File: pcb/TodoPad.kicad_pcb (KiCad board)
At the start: 2 copper layers, 30 parts, among them SW1 SW_Push, SW10 SW_Push, SW11 SW_Push, SW12 SW_Push, SW13 SW_Push, SW14 SW_Push, SW2 SW_Push, SW3 SW_Push, SW4 SW_Push, SW5 SW_Push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

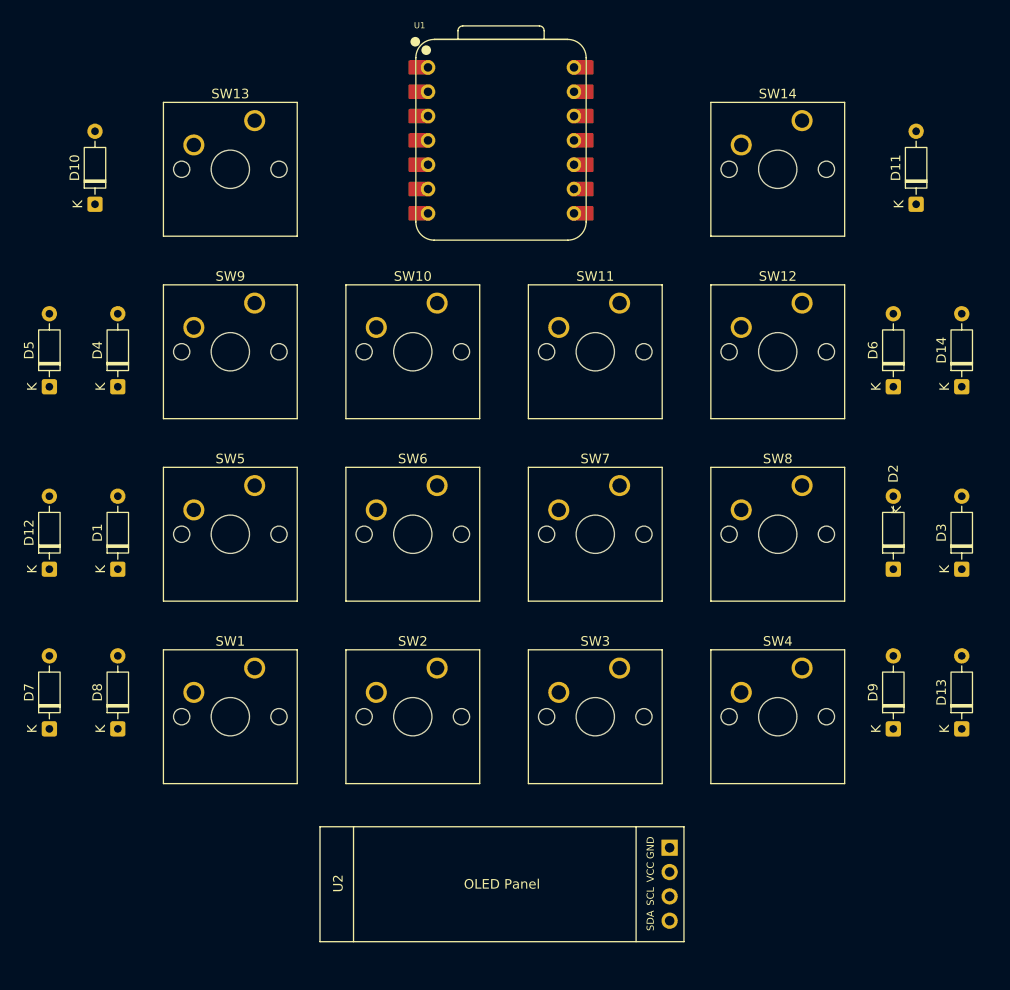
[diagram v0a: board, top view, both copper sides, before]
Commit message: Started routing PCB
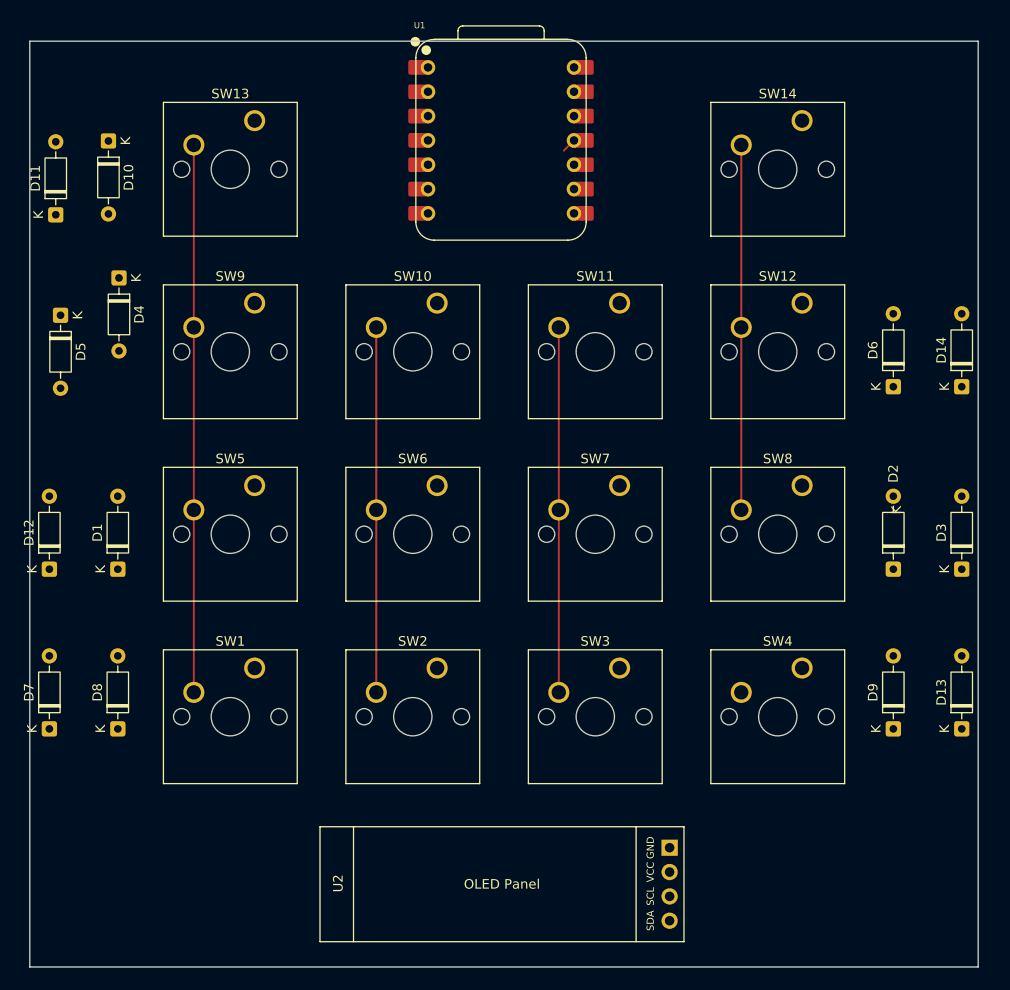
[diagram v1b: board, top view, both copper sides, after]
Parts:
- moved D11 89.8 mm to (92.7, 64.6)
- moved D4 11.4 mm to (99.3, 71.2), turned to -90 degrees
- moved D5 7.55 mm to (93.2, 75.1), turned to -90 degrees
- moved D10 6.76 mm to (98.2, 56.9), turned to -90 degrees
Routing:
- net Col 0: track 0.00 -> 58.7 mm
- net Col 3: track 0.00 -> 38.5 mm
- net Col 2: track 0.00 -> 38.1 mm
- net Col 1: track 0.00 -> 38.1 mm
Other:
- board outline added: 99 x 96.7 mm
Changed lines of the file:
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@@
 	(footprint "Diode_THT:D_DO-35_SOD27_P7.62mm_Horizontal"
 		(layer "F.Cu")
-		(at 99.1775 82.55 90)
+		(at 99.3 71.19 -90)
 		(descr "Diode, DO-35_SOD27 series, Axial, Horizontal, pin pitch=7.62mm, length*diameter=4*2mm^2, http://www.diodes.com/_files/packages/DO-35.pdf")
 		(tags "Diode DO-35_SOD27 series Axial Horizontal pin pitch 7.62mm  length 4mm diameter 2mm")
@@
 		)
 		(property "Sim.Device" "D"
-			(at 0 0 90)
+			(at 0 0 270)
 			(unlocked yes)
 			(layer "F.Fab")
@@
 		)
 		(property "Sim.Pins" "1=K 2=A"
-			(at 0 0 90)
+			(at 0 0 270)
 			(unlocked yes)
 			(layer "F.Fab")
@@
 		(attr through_hole)
 		(fp_line
-			(start 2.53 -1.12)
-			(end 2.53 1.12)
+			(start 1.04 0)
+			(end 1.69 0)
 			(stroke
 				(width 0.12)
@@
 		)
 		(fp_line
-			(start 2.41 -1.12)
-			(end 2.41 1.12)
+			(start 6.58 0)
+			(end 5.93 0)
 			(stroke
 				(width 0.12)
@@
 		)
 		(fp_line
-			(start 6.58 0)
-			(end 5.93 0)
+			(start 2.41 -1.12)
+			(end 2.41 1.12)
 			(stroke
 				(width 0.12)
@@
 		)
 		(fp_line
-			(start 1.04 0)
-			(end 1.69 0)
+			(start 2.53 -1.12)
+			(end 2.53 1.12)
 			(stroke
 				(width 0.12)
@@
 		)
 		(fp_line
-			(start 2.51 -1)
-			(end 2.51 1)
+			(start 0 0)
+			(end 1.81 0)
 			(stroke
 				(width 0.1)
@@
 		)
 		(fp_line
-			(start 2.41 -1)
-			(end 2.41 1)
+			(start 7.62 0)
+			(end 5.81 0)
 			(stroke
 				(width 0.1)
@@
 		)
 		(fp_line
-			(start 7.62 0)
-			(end 5.81 0)
+			(start 2.41 -1)
+			(end 2.41 1)
 			(stroke
 				(width 0.1)
@@
 		)
 		(fp_line
-			(start 0 0)
-			(end 1.81 0)
+			(start 2.51 -1)
+			(end 2.51 1)
 			(stroke
 				(width 0.1)
@@
 		)
 		(pad "1" thru_hole roundrect
-			(at 0 0 90)
+			(at 0 0 270)
 			(size 1.6 1.6)
 			(drill 0.8)
@@
 		)
 		(pad "2" thru_hole circle
-			(at 7.62 0 90)
+			(at 7.62 0 270)
 			(size 1.6 1.6)
 			(drill 0.8)
@@
 	(footprint "Diode_THT:D_DO-35_SOD27_P7.62mm_Horizontal"
 		(layer "F.Cu")
-		(at 96.79625 63.5 90)
+		(at 98.2 56.89 -90)
 		(descr "Diode, DO-35_SOD27 series, Axial, Horizontal, pin pitch=7.62mm, length*diameter=4*2mm^2, http://www.diodes.com/_files/packages/DO-35.pdf")
 		(tags "Diode DO-35_SOD27 series Axial Horizontal pin pitch 7.62mm  length 4mm diameter 2mm")
@@
 		)
 		(property "Sim.Device" "D"
-			(at 0 0 90)
+			(at 0 0 270)
 			(unlocked yes)
 			(layer "F.Fab")
@@
 		)
 		(property "Sim.Pins" "1=K 2=A"
-			(at 0 0 90)
+			(at 0 0 270)
 			(unlocked yes)
 			(layer "F.Fab")
@@
 		(attr through_hole)
 		(fp_line
-			(start 2.53 -1.12)
-			(end 2.53 1.12)
+			(start 1.04 0)
+			(end 1.69 0)
 			(stroke
 				(width 0.12)
@@
 		)
 		(fp_line
-			(start 2.41 -1.12)
-			(end 2.41 1.12)
+			(start 6.58 0)
+			(end 5.93 0)
 			(stroke
 				(width 0.12)
@@
 		)
 		(fp_line
-			(start 6.58 0)
-			(end 5.93 0)
+			(start 2.41 -1.12)
+			(end 2.41 1.12)
 			(stroke
 				(width 0.12)
@@
 		)
 		(fp_line
-			(start 1.04 0)
-			(end 1.69 0)
+			(start 2.53 -1.12)
+			(end 2.53 1.12)
 			(stroke
 				(width 0.12)
@@
 		)
 		(fp_line
-			(start 2.51 -1)
-			(end 2.51 1)
+			(start 0 0)
+			(end 1.81 0)
 			(stroke
 				(width 0.1)
@@
 		)
 		(fp_line
-			(start 2.41 -1)
-			(end 2.41 1)
+			(start 7.62 0)
+			(end 5.81 0)
 			(stroke
 				(width 0.1)
@@
 		)
 		(fp_line
-			(start 7.62 0)
-			(end 5.81 0)
+			(start 2.41 -1)
+			(end 2.41 1)
 			(stroke
 				(width 0.1)
@@
 		)
 		(fp_line
-			(start 0 0)
-			(end 1.81 0)
+			(start 2.51 -1)
+			(end 2.51 1)
 			(stroke
 				(width 0.1)
@@
 		)
 		(pad "1" thru_hole roundrect
-			(at 0 0 90)
+			(at 0 0 270)
 			(size 1.6 1.6)
 			(drill 0.8)
@@
 		)
 		(pad "2" thru_hole circle
-			(at 7.62 0 90)
+			(at 7.62 0 270)
 			(size 1.6 1.6)
 			(drill 0.8)
@@
 	(footprint "Diode_THT:D_DO-35_SOD27_P7.62mm_Horizontal"
 		(layer "F.Cu")
-		(at 182.52125 63.5 90)
+		(at 92.7 64.6 90)
 		(descr "Diode, DO-35_SOD27 series, Axial, Horizontal, pin pitch=7.62mm, length*diameter=4*2mm^2, http://www.diodes.com/_files/packages/DO-35.pdf")
 		(tags "Diode DO-35_SOD27 series Axial Horizontal pin pitch 7.62mm  length 4mm diameter 2mm")
@@
 	(footprint "Diode_THT:D_DO-35_SOD27_P7.62mm_Horizontal"
 		(layer "F.Cu")
-		(at 92.03375 82.55 90)
+		(at 93.2 75.09 -90)
 		(descr "Diode, DO-35_SOD27 series, Axial, Horizontal, pin pitch=7.62mm, length*diameter=4*2mm^2, http://www.diodes.com/_files/packages/DO-35.pdf")
 		(tags "Diode DO-35_SOD27 series Axial Horizontal pin pitch 7.62mm  length 4mm diameter 2mm")
@@
 		)
 		(property "Sim.Device" "D"
-			(at 0 0 90)
+			(at 0 0 270)
 			(unlocked yes)
 			(layer "F.Fab")
@@
 		)
 		(property "Sim.Pins" "1=K 2=A"
-			(at 0 0 90)
+			(at 0 0 270)
 			(unlocked yes)
 			(layer "F.Fab")
@@
 		(attr through_hole)
 		(fp_line
-			(start 2.53 -1.12)
-			(end 2.53 1.12)
+			(start 1.04 0)
+			(end 1.69 0)
 			(stroke
 				(width 0.12)
@@
 		)
 		(fp_line
-			(start 2.41 -1.12)
-			(end 2.41 1.12)
+			(start 6.58 0)
+			(end 5.93 0)
 			(stroke
 				(width 0.12)
@@
 		)
 		(fp_line
-			(start 6.58 0)
-			(end 5.93 0)
+			(start 2.41 -1.12)
+			(end 2.41 1.12)
 			(stroke
 				(width 0.12)
@@
 		)
 		(fp_line
-			(start 1.04 0)
-			(end 1.69 0)
+			(start 2.53 -1.12)
+			(end 2.53 1.12)
 			(stroke
 				(width 0.12)
@@
 		)
 		(fp_line
-			(start 2.51 -1)
-			(end 2.51 1)
+			(start 0 0)
+			(end 1.81 0)
 			(stroke
 				(width 0.1)
@@
 		)
 		(fp_line
-			(start 2.41 -1)
-			(end 2.41 1)
+			(start 7.62 0)
+			(end 5.81 0)
 			(stroke
 				(width 0.1)
@@
 		)
 		(fp_line
-			(start 7.62 0)
-			(end 5.81 0)
+			(start 2.41 -1)
+			(end 2.41 1)
 			(stroke
 				(width 0.1)
@@
 		)
 		(fp_line
-			(start 0 0)
-			(end 1.81 0)
+			(start 2.51 -1)
+			(end 2.51 1)
 			(stroke
 				(width 0.1)
@@
 		)
 		(pad "1" thru_hole roundrect
-			(at 0 0 90)
+			(at 0 0 270)
 			(size 1.6 1.6)
 			(drill 0.8)
@@
 		)
 		(pad "2" thru_hole circle
-			(at 7.62 0 90)
+			(at 7.62 0 270)
 			(size 1.6 1.6)
 			(drill 0.8)
@@
 		)
 	)
+	(gr_rect
+		(start 89.9875 46.475)
+		(end 189 143.125)
+		(stroke
+			(width 0.05)
+			(type default)
+		)
+		(fill no)
+		(layer "Edge.Cuts")
+	)
+	(segment
+		(start 146.8025 56.8325)
+		(end 145.7395 57.8955)
+		(width 0.2)
+		(layer "F.Cu")
+		(net 19)
+	)
+	(segment
+		(start 107.115 57.30875)
+		(end 107.115 76.35875)
+		(width 0.2)
+		(layer "F.Cu")
+		(net 19)
+	)
+	(segment
+		(start 107.115 95.40875)
+		(end 107.115 114.45875)
+		(width 0.2)
+		(layer "F.Cu")
+		(net 19)
+	)
+	(segment
+		(start 107.115 76.35875)
+		(end 107.115 95.40875)
+		(width 0.2)
+		(layer "F.Cu")
+		(net 19)
+	)
+	(segment
+		(start 126.165 95.40875)
+		(end 126.165 114.45875)
+		(width 0.2)
+		(layer "F.Cu")
+		(net 20)
+	)
+	(segment
+		(start 126.165 76.35875)
+		(end 126.165 95.40875)
+		(width 0.2)
+		(layer "F.Cu")
+		(net 20)
+	)
+	(segment
+		(start 145.215 95.40875)
+		(end 145.215 114.45875)
+		(width 0.2)
+		(layer "F.Cu")
+		(net 21)
+	)
+	(segment
+		(start 145.215 76.35875)
+		(end 145.215 95.40875)
+		(width 0.2)
+		(layer "F.Cu")
+		(net 21)
+	)
+	(segment
+		(start 163.83653 57.30875)
+		(end 164.265 57.30875)
+		(width 0.2)
+		(layer "F.Cu")
+		(net 22)
+	)
+	(segment
+		(start 164.265 57.30875)
+		(end 164.265 76.35875)
+		(width 0.2)
+		(layer "F.Cu")
+		(net 22)
+	)
+	(segment
+		(start 164.265 76.35875)
+		(end 164.265 95.40875)
+		(width 0.2)
+		(layer "F.Cu")
+		(net 22)
+	)
 	(embedded_fonts no)

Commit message: Routing first attempt is complete
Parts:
- moved D12 88.6 mm to (180.5, 106.7)
- moved D2 86.3 mm to (94.0, 95.9)
- moved D10 27.2 mm to (125.1, 52.8)
- moved D11 8.70 mm to (95.9, 56.5)
- moved D9 7.65 mm to (180.4, 125.9)
- moved D8 6.52 mm to (97.3, 124.5)
- moved D6 4.22 mm to (181.3, 78.5), turned to -90 degrees
- moved D7 2.97 mm to (93.7, 115.8)
- moved D13 1.23 mm to (186.3, 119.0)
- moved D4 1.09 mm to (98.7, 70.3)
- moved D1 0.99 mm to (98.8, 102.5)
- moved D5 0.89 mm to (92.4, 74.7)
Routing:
- net Row 3: track 0.00 -> 207.4 mm, vias 0 -> 1
- net Row 2: track 0.00 -> 181.6 mm
- net Row 1: track 0.00 -> 129.8 mm
- net +5V: track 0.00 -> 111.0 mm
- net Net-(U1-GPIO6/SDA): track 0.00 -> 104.1 mm
- net Net-(U1-GPIO7/SCL): track 0.00 -> 99.7 mm
- net GND: track 0.00 -> 98.6 mm
- net Net-(D11-A): track 0.00 -> 77.8 mm
- net Net-(D5-A): track 0.00 -> 43.6 mm
- net Net-(D2-A): track 0.00 -> 40.4 mm
- net Net-(D8-A): track 0.00 -> 39.3 mm
- net Col 0: track 58.7 -> 97.5 mm
- net Row 0: track 0.00 -> 38.7 mm
- net Net-(D3-A): track 0.00 -> 37.3 mm
- net Net-(D6-A): track 0.00 -> 34.8 mm
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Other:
- board size 99 x 96.7 mm -> 99 x 97.2 mm
- board text added: "Todo Pad"
- board text added: "XIAO HERE"

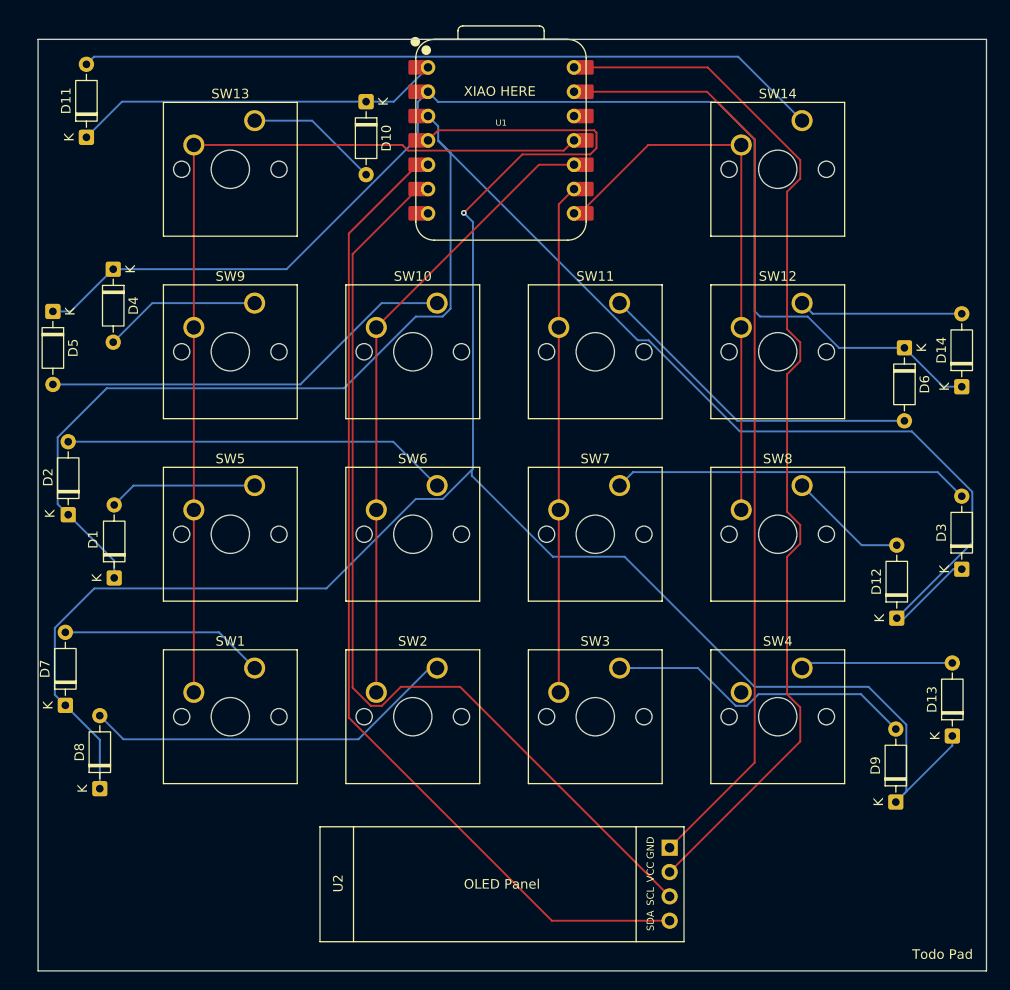
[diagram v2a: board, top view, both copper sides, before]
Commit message: Add decorations and branding to PCB
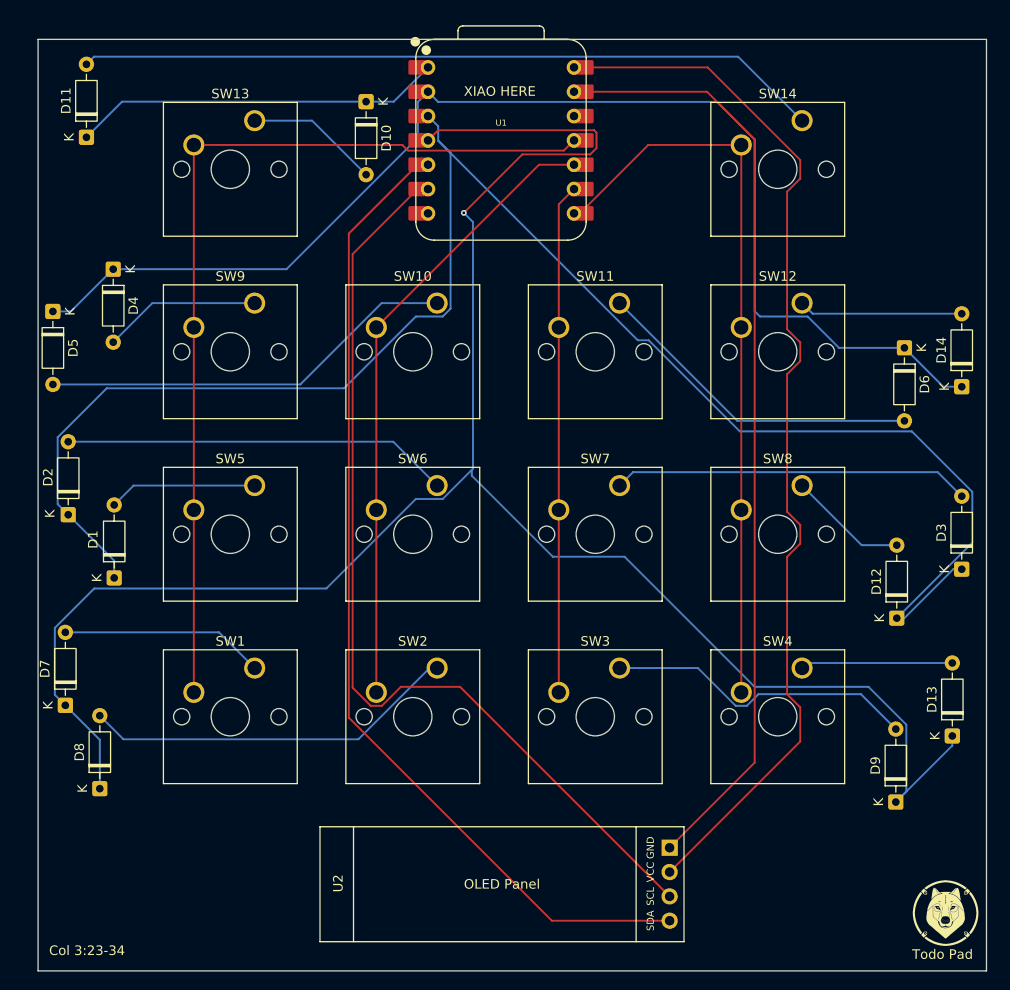
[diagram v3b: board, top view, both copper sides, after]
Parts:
- added G***: LOGO, Icons:wolfIcon, F.Cu at (185.6, 137.5)
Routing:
- net Col 3: track 58.5 -> 77.6 mm
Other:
- board text added: "Col 3:23-34"

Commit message: Centred PCB components, started case model
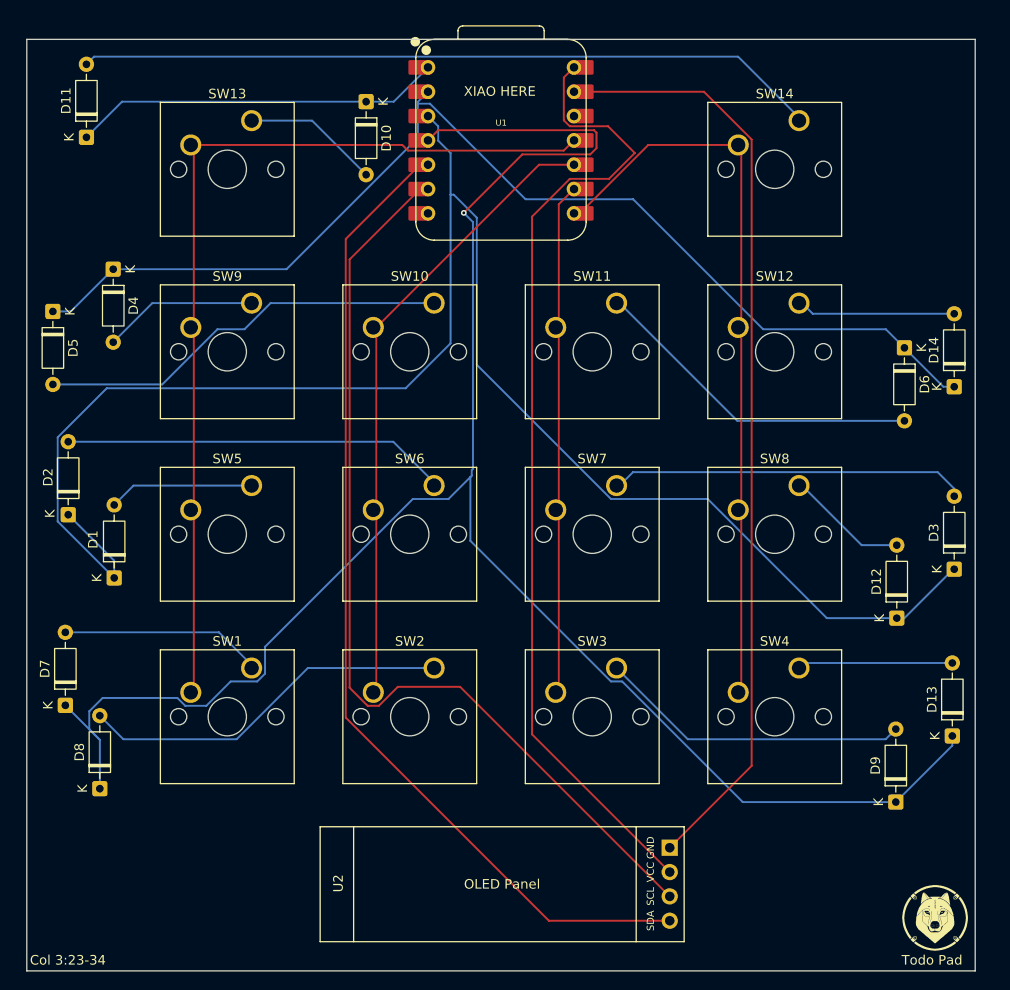
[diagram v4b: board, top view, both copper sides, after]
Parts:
- moved G*** 1.21 mm to (184.5, 138.0)
- moved D14 0.78 mm to (186.5, 82.5)
- moved D3 0.78 mm to (186.5, 101.6)
- moved SW1 0.32 mm to (113.1, 111.9)
- moved SW13 0.32 mm to (113.1, 54.8)
- moved SW5 0.32 mm to (113.1, 92.9)
- moved SW9 0.32 mm to (113.1, 73.8)
- moved SW10 0.32 mm to (132.2, 73.8)
- moved SW11 0.32 mm to (151.2, 73.8)
- moved SW12 0.32 mm to (170.3, 73.8)
- moved SW14 0.32 mm to (170.3, 54.8)
- moved SW2 0.32 mm to (132.2, 111.9)
- moved SW3 0.32 mm to (151.2, 111.9)
- moved SW4 0.32 mm to (170.3, 111.9)
- moved SW6 0.32 mm to (132.2, 92.9)
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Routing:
- net Row 1: track 129.8 -> 119.1 mm
- net +5V: track 111.0 -> 102.6 mm
- net Row 3: track 207.4 -> 202.1 mm
- net Row 2: track 181.6 -> 178.0 mm
- net Net-(D14-A): track 17.1 -> 16.3 mm
- net Net-(U1-GPIO7/SCL): track 99.7 -> 99.2 mm
